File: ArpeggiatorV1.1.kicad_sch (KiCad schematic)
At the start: 61 parts, among them J1 DIN-5_180degree, J2 DIN-5_180degree, J3 DIN-5_180degree, J4 Conn_01x03_Pin, SW1 SW_MEC_5E, SW2 SW_MEC_5E, SW3 SW_MEC_5E, SW4 SW_MEC_5E, SW5 SW_MEC_5E, U1 Pico, U2 6N138, U3 6N138

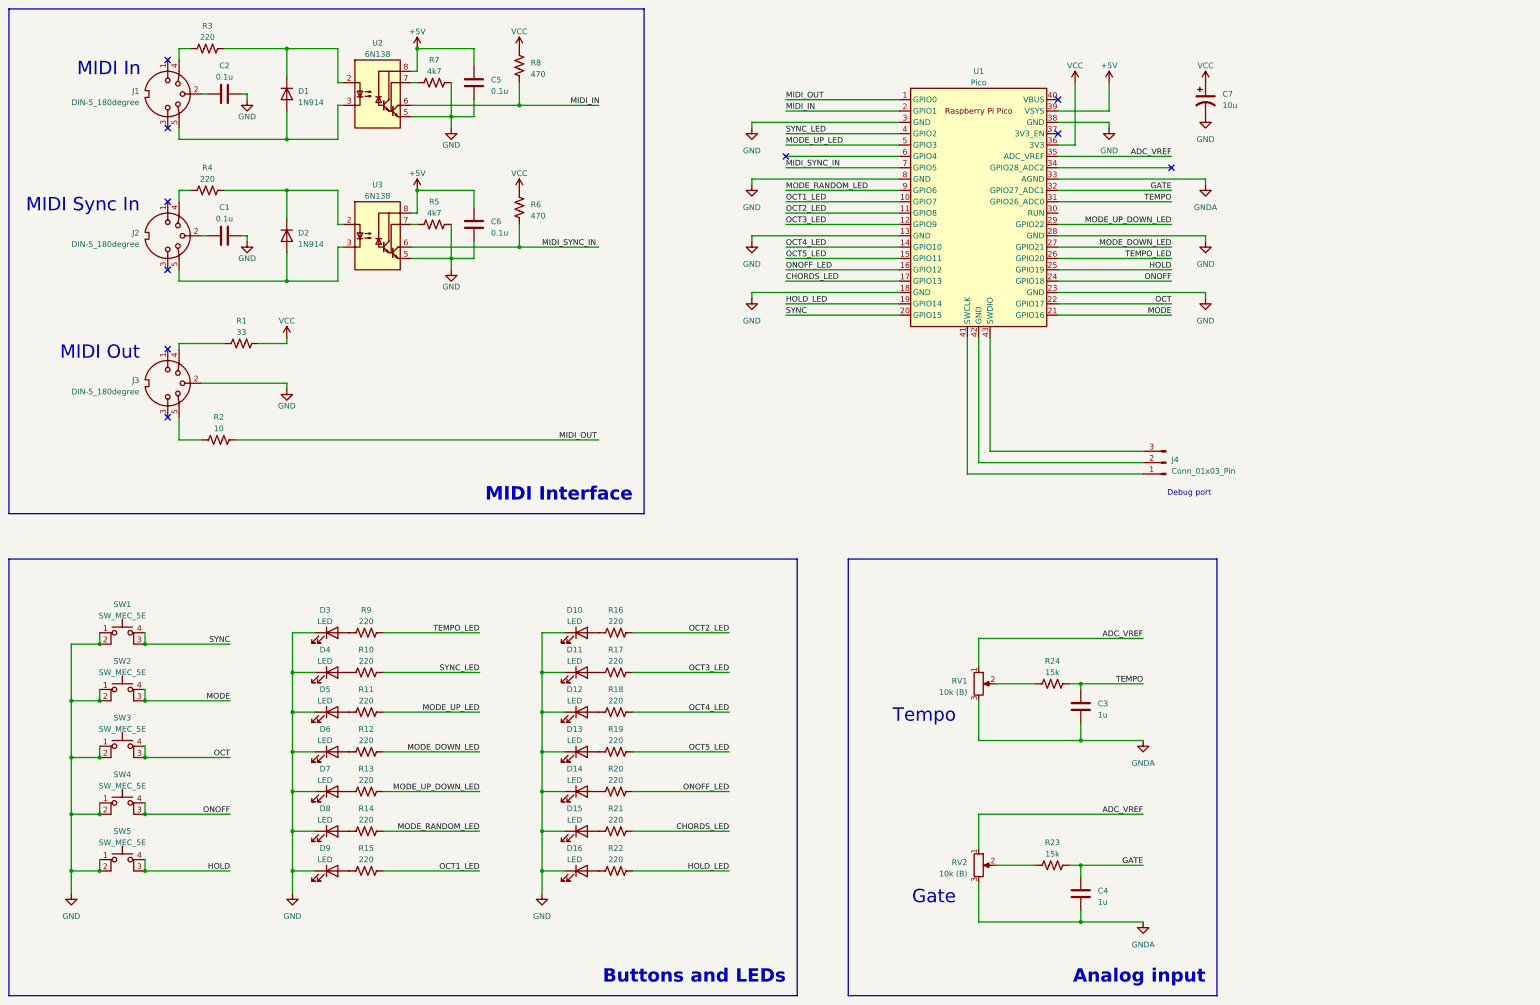
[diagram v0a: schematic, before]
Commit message: Cleaned up schematic
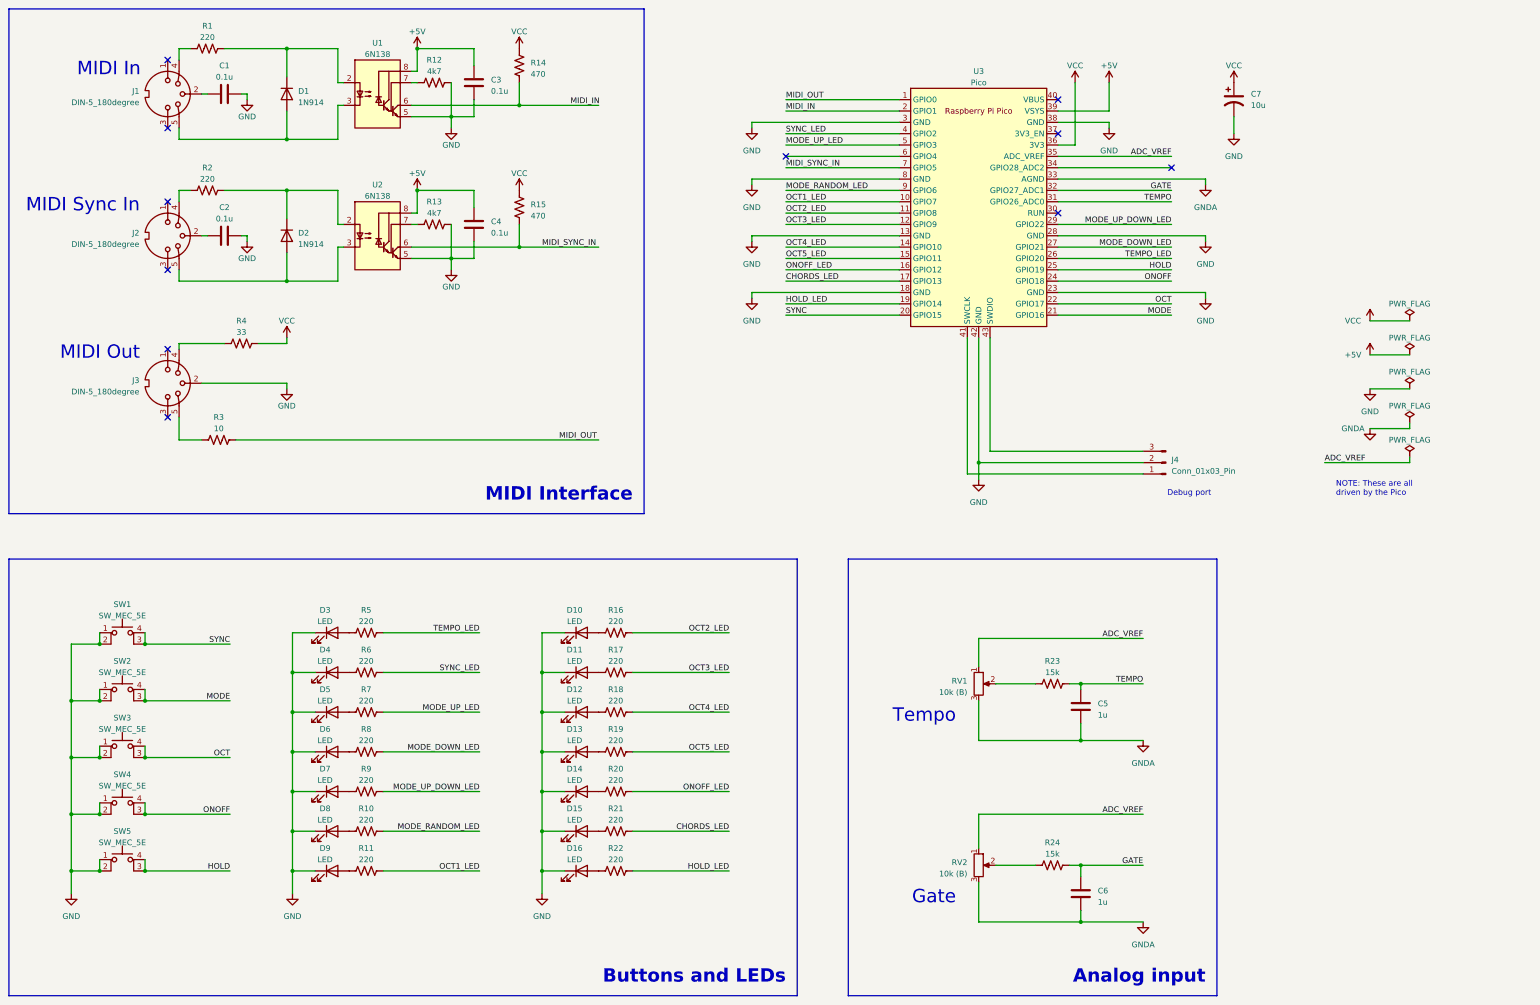
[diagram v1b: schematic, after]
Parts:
- renumbered C2 to C1, C1 to C2, C5 to C3, C6 to C4, C3 to C5, C4 to C6, R3 to R1, R14 to R10, R15 to R11, R7 to R12, R5 to R13, R8 to R14, R6 to R15, R4 to R2, R24 to R23, R23 to R24, R2 to R3, R1 to R4, R9 to R5, R10 to R6, R11 to R7, R12 to R8, R13 to R9, U2 to U1, U3 to U2, U1 to U3
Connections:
- net GND: now also J4.2 (Pin_2), U3.42 (GND)
- no-connect marks 10 -> 11
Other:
- note added: "NOTE: These are all driven by the Pico"
- moved on the sheet: C7

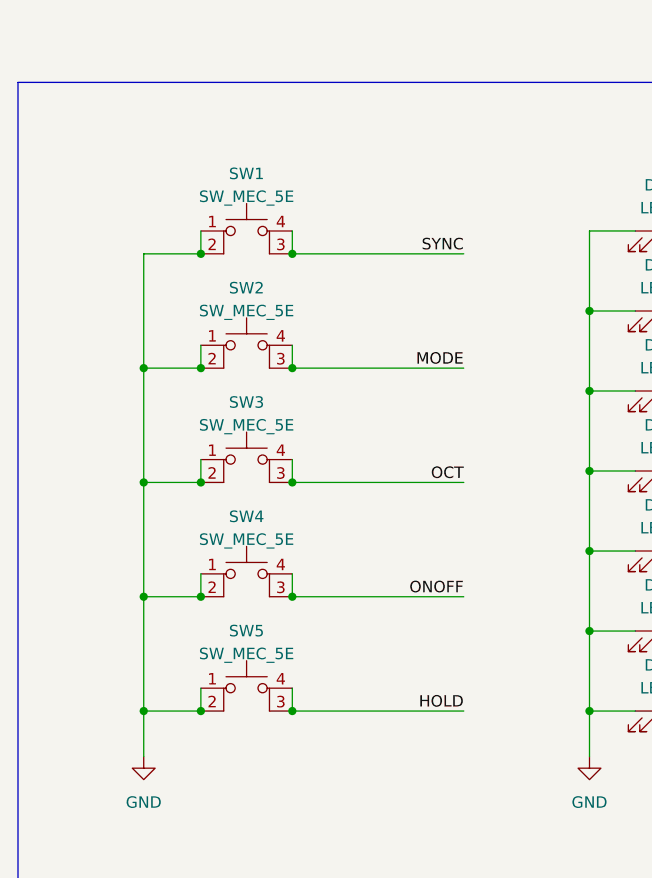
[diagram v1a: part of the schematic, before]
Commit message: Updated component footprints. Set initial PCB design rules for common prototyping houses like PCBWay and OSHPark.
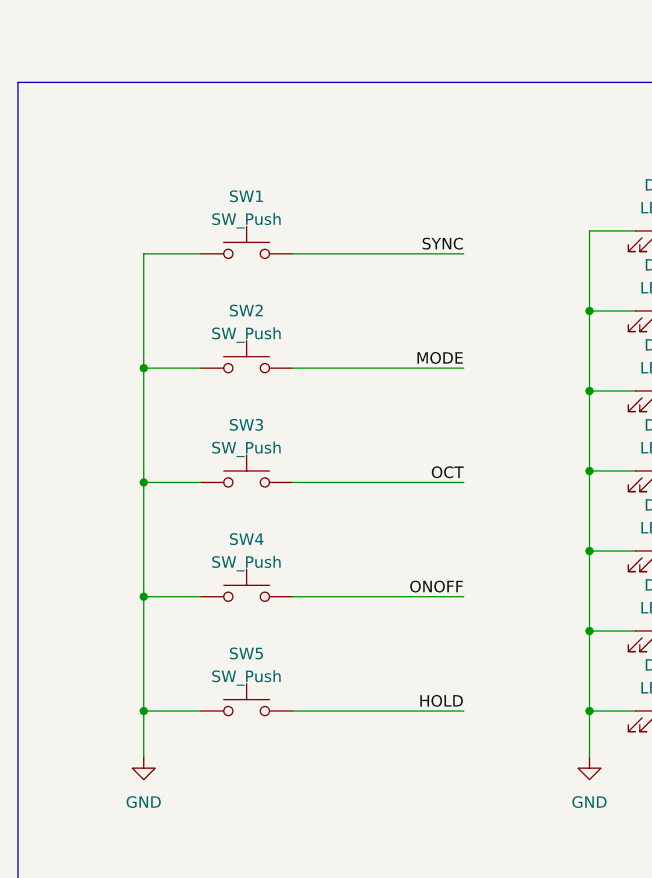
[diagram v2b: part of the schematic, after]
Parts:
- removed SW1, SW2, SW3, SW4, SW5: SW_MEC_5E, symbol Switch:SW_MEC_5E
- added SW1, SW2, SW3, SW4, SW5: SW_Push, Button_Switch_THT:SW_PUSH_6mm, symbol Switch:SW_Push
- C1, C2, C3, C4, C5, C6: footprint (none) -> Capacitor_THT:C_Disc_D3.0mm_W1.6mm_P2.50mm
- C7: footprint (none) -> Capacitor_THT:CP_Radial_D5.0mm_P2.50mm
- D1, D2: footprint (none) -> Diode_THT:D_A-405_P7.62mm_Horizontal
- D10, D11, D12, D13, D14, D15, D16, D3, D4, D5, D6, D7, D8, D9: footprint (none) -> LED_THT:LED_D3.0mm
- J1, J2, J3: footprint (none) -> Eurocad:MIDI_DIN5
- J4, R1, R10, R11, R12, R13, R14, R15, R16, R17, R18, R19, R2, R20, R21, R22, R23, R24, R3, R4, R5, R6, R7, R8, R9: footprint (none) -> Resistor_THT:R_Axial_DIN0207_L6.3mm_D2.5mm_P10.16mm_Horizontal
- RV1, RV2: footprint (none) -> Connector_PinHeader_2.54mm:PinHeader_1x03_P2.54mm_Vertical
- U1, U2: footprint (none) -> Package_DIP:DIP-8_W7.62mm_LongPads
- U3: footprint RPi_Pico:RPi_Pico_SMD_TH -> MCU_RaspberryPi_and_Boards:RPi_Pico_SMD_TH
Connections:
- net GND: now also SW1.1, SW2.1, SW3.1, SW4.1, SW5.1
- net HOLD: now also SW5.2
- net MODE: now also SW2.2
- net OCT: now also SW3.2
- net ONOFF: now also SW4.2
- net SYNC: now also SW1.2

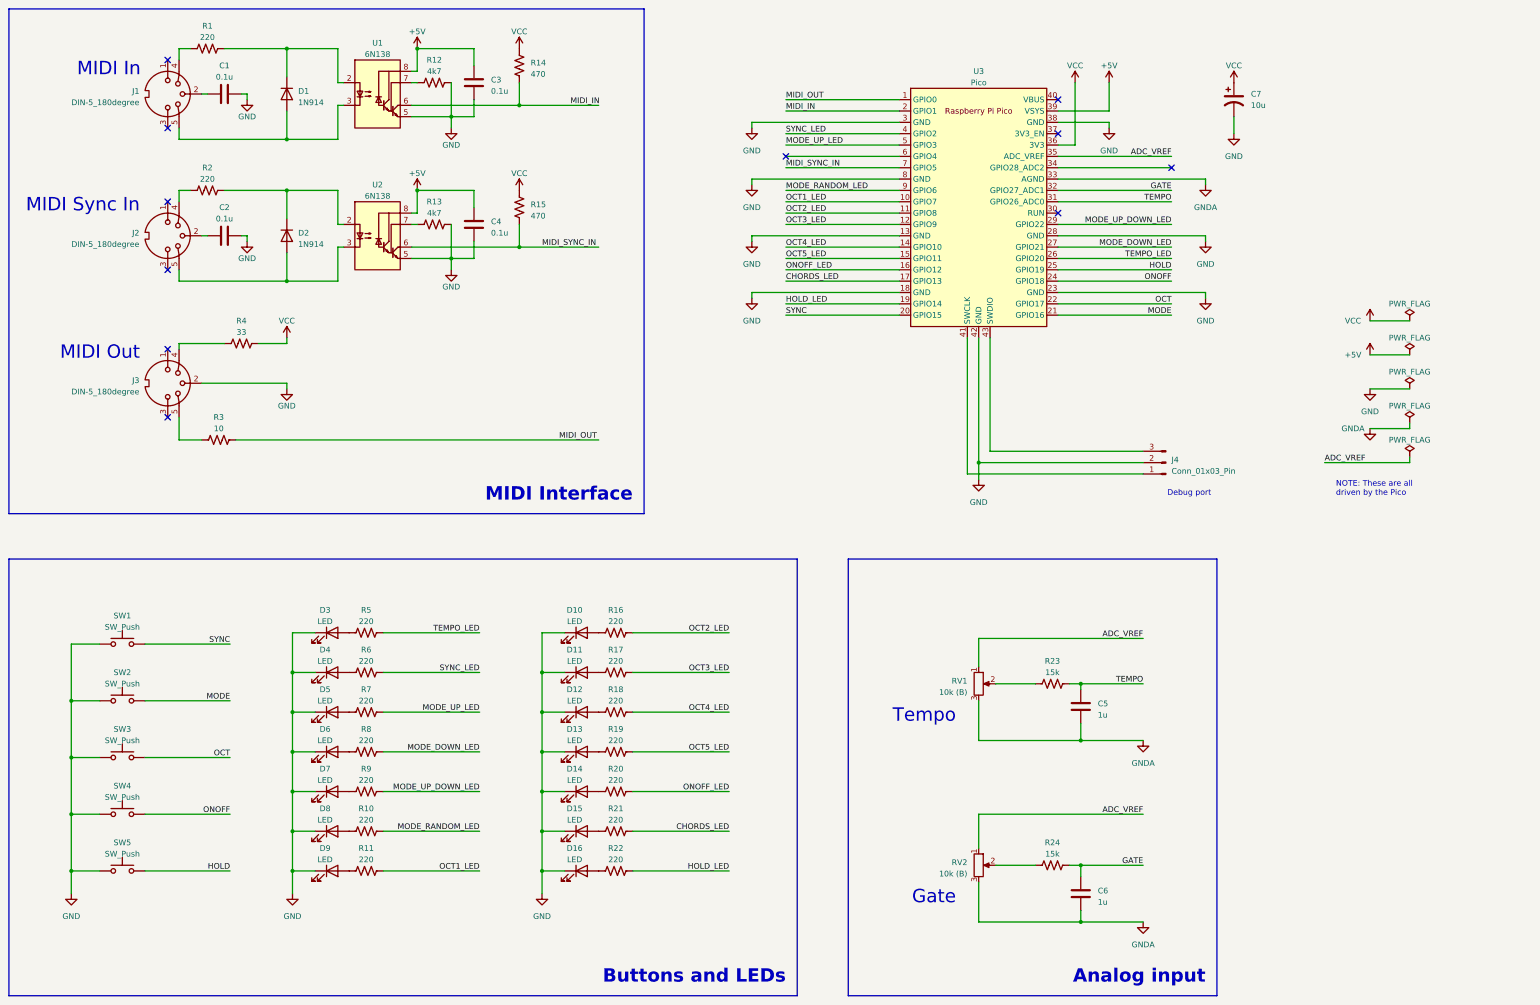
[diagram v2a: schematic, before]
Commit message: Adjusted pin assigments for a cleaner layout. Partially laid out and routed board.
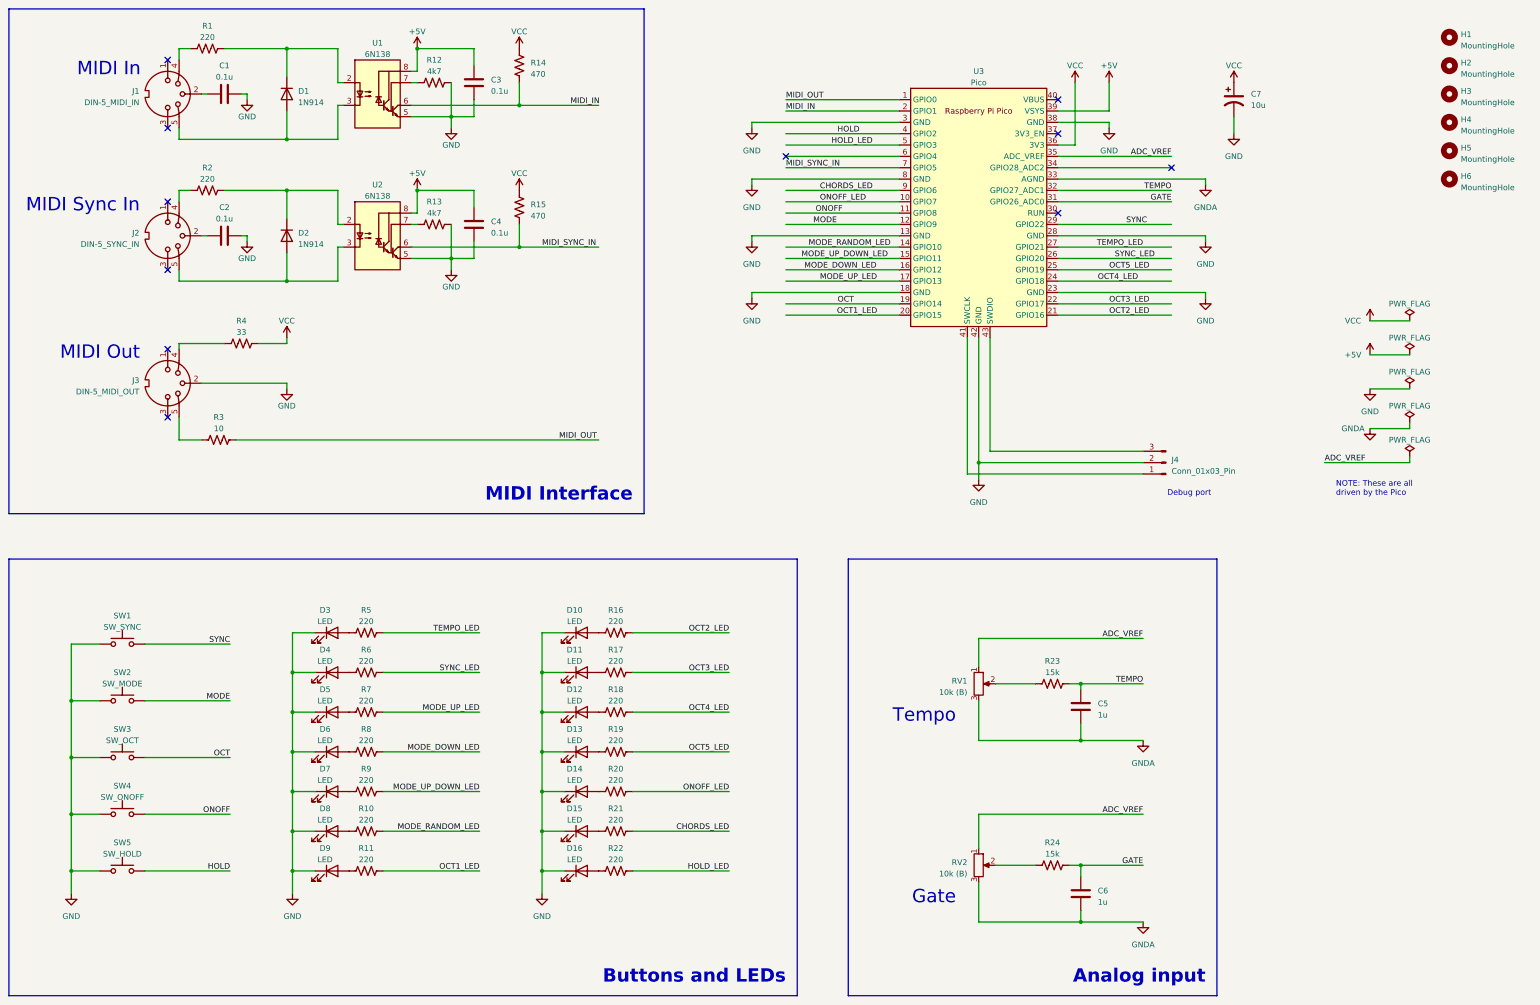
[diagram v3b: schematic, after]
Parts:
- added H1, H2, H3, H4, H5, H6: MountingHole, MountingHole:MountingHole_4mm, symbol Mechanical:MountingHole
- J1: value DIN-5_180degree -> DIN-5_MIDI_IN
- J2: value DIN-5_180degree -> DIN-5_SYNC_IN
- J3: value DIN-5_180degree -> DIN-5_MIDI_OUT
- J4: footprint Resistor_THT:R_Axial_DIN0207_L6.3mm_D2.5mm_P10.16mm_Horizontal -> Connector_PinHeader_2.54mm:PinHeader_1x03_P2.54mm_Horizontal
- SW1: value SW_Push -> SW_SYNC
- SW2: value SW_Push -> SW_MODE
- SW3: value SW_Push -> SW_OCT
- SW4: value SW_Push -> SW_ONOFF
- SW5: value SW_Push -> SW_HOLD
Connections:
- net CHORDS_LED: now also U3.9 (GPIO6); no longer U3.17 (GPIO13)
- net GATE: now also U3.31 (GPIO26_ADC0); no longer U3.32 (GPIO27_ADC1)
- net HOLD: now also U3.4 (GPIO2); no longer U3.25 (GPIO19)
- net HOLD_LED: now also U3.5 (GPIO3); no longer U3.19 (GPIO14)
- net MODE: now also U3.12 (GPIO9); no longer U3.21 (GPIO16)
- net MODE_DOWN_LED: now also U3.16 (GPIO12); no longer U3.27 (GPIO21)
- net MODE_RANDOM_LED: now also U3.14 (GPIO10); no longer U3.9 (GPIO6)
- net MODE_UP_DOWN_LED: now also U3.15 (GPIO11); no longer U3.29 (GPIO22)
- net MODE_UP_LED: now also U3.17 (GPIO13); no longer U3.5 (GPIO3)
- net OCT: now also U3.19 (GPIO14); no longer U3.22 (GPIO17)
- net OCT1_LED: now also U3.20 (GPIO15); no longer U3.10 (GPIO7)
- net OCT2_LED: now also U3.21 (GPIO16); no longer U3.11 (GPIO8)
- net OCT3_LED: now also U3.22 (GPIO17); no longer U3.12 (GPIO9)
- net OCT4_LED: now also U3.24 (GPIO18); no longer U3.14 (GPIO10)
- net OCT5_LED: now also U3.25 (GPIO19); no longer U3.15 (GPIO11)
- net ONOFF: now also U3.11 (GPIO8); no longer U3.24 (GPIO18)
- net ONOFF_LED: now also U3.10 (GPIO7); no longer U3.16 (GPIO12)
- net SYNC: now also U3.29 (GPIO22); no longer U3.20 (GPIO15)
- net SYNC_LED: now also U3.26 (GPIO20); no longer U3.4 (GPIO2)
- net TEMPO: now also U3.32 (GPIO27_ADC1); no longer U3.31 (GPIO26_ADC0)
- net TEMPO_LED: now also U3.27 (GPIO21); no longer U3.26 (GPIO20)
